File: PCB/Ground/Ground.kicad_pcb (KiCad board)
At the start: 2 copper layers, 100 x 86.6 mm, 39 parts, among them CN1 GROVE, CN2 GROVE, CN3 GROVE, CN4 GROVE, CN5 GROVE, CN6 TTL-232R-3V3, CN7 ST-LINK, CN8 Conn_01x05_Female, CN9 CardEdgeConnector5P, SW1 RESET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

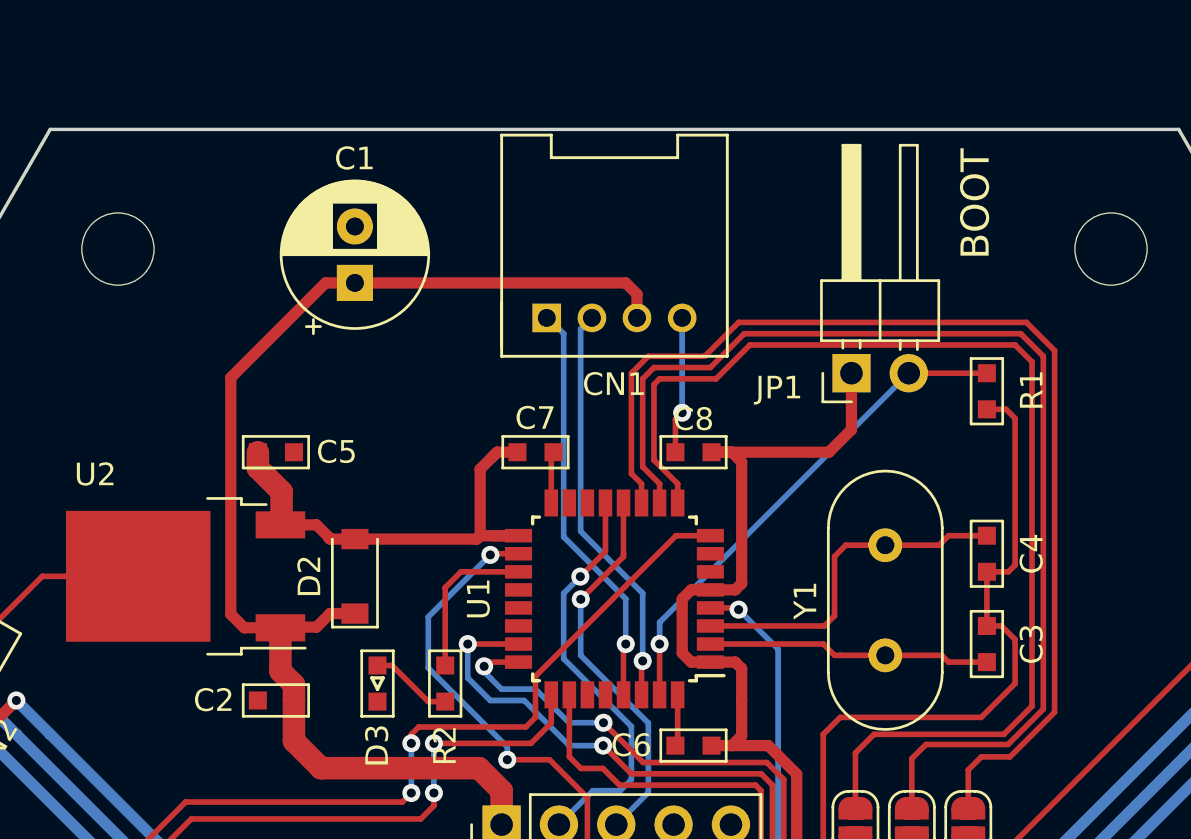
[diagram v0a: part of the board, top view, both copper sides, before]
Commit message: [update] Groundの配線改善(+5V配線, BOOT) #4
* C5(レギュレータ直近)を反転
* +5V配線幅を0.5mmから1.0mmに拡大
* JP1(BOOT)にOPEN/SHORTそれぞれの機能をシルクで記載
  (RUN/BOOT)
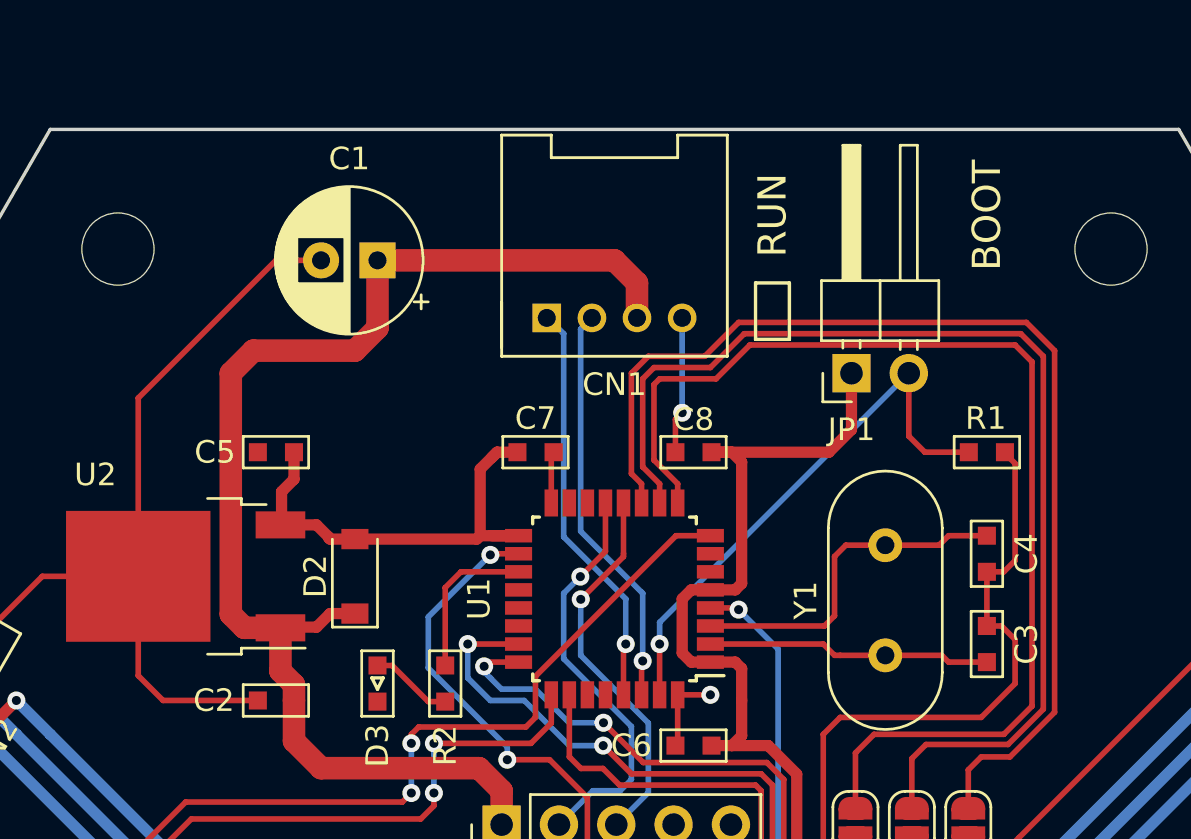
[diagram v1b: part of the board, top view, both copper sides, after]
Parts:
- moved R1 2.70 mm to (146.5, 76.0), turned to 0 degrees
- moved C1 1.41 mm to (119.5, 67.5), turned to 180 degrees
- turned C5 to 180 degrees
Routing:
- net GND: track 116.5 -> 143.8 mm, vias 1 -> 2
- net 5V: track 220.4 -> 223.4 mm
- net Net-(JP1-Pad2): track 22.3 -> 24.6 mm
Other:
- board text added: "RUN"

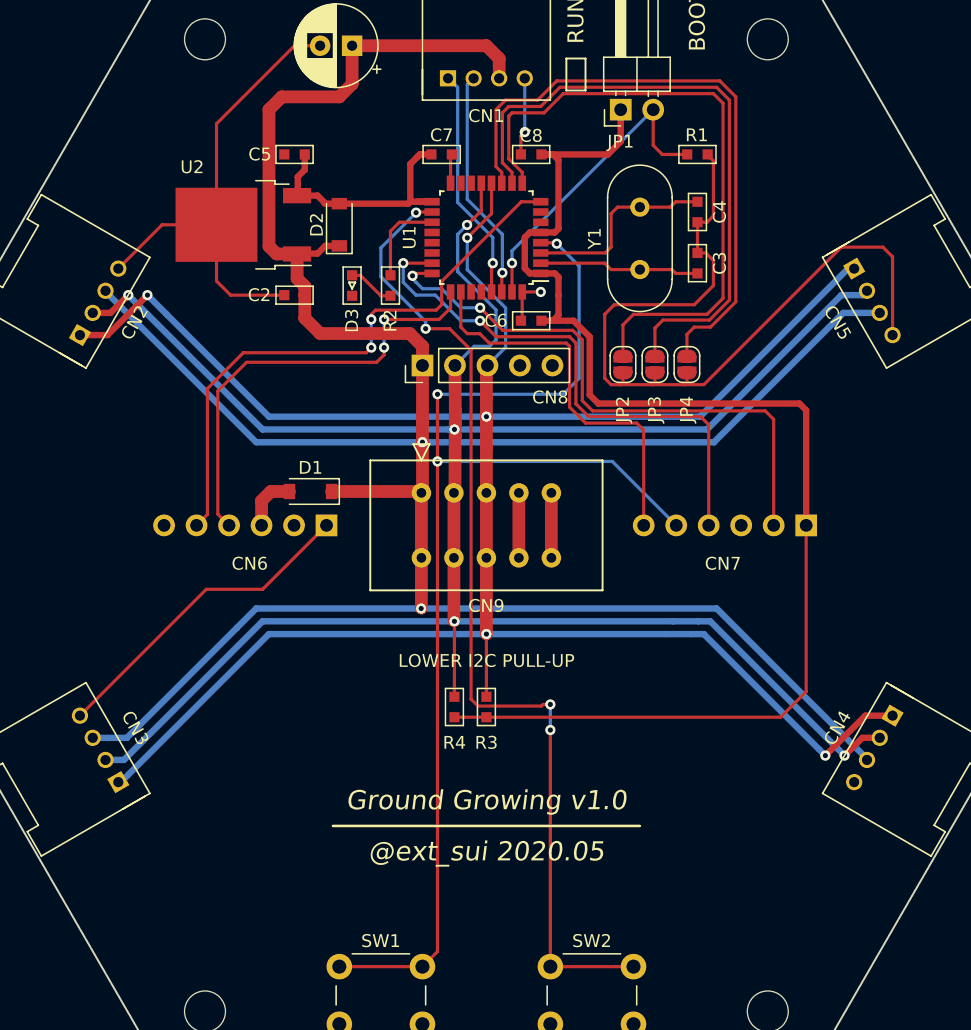
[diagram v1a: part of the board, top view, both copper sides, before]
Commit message: [update] Groundの配線改善(3V3配線, シルク) #4
* IC周辺の3V3配線を他の配線より優先するように修正
* I2C関連のコネクタ部の裏側にシルクを追加
* JP2-4の配線を表面から裏面に変更し配線長を短縮
* ST-LINK関連の配線を下に移動しGNDベタ用ビアを追加
* IC周辺のビア位置を整頓
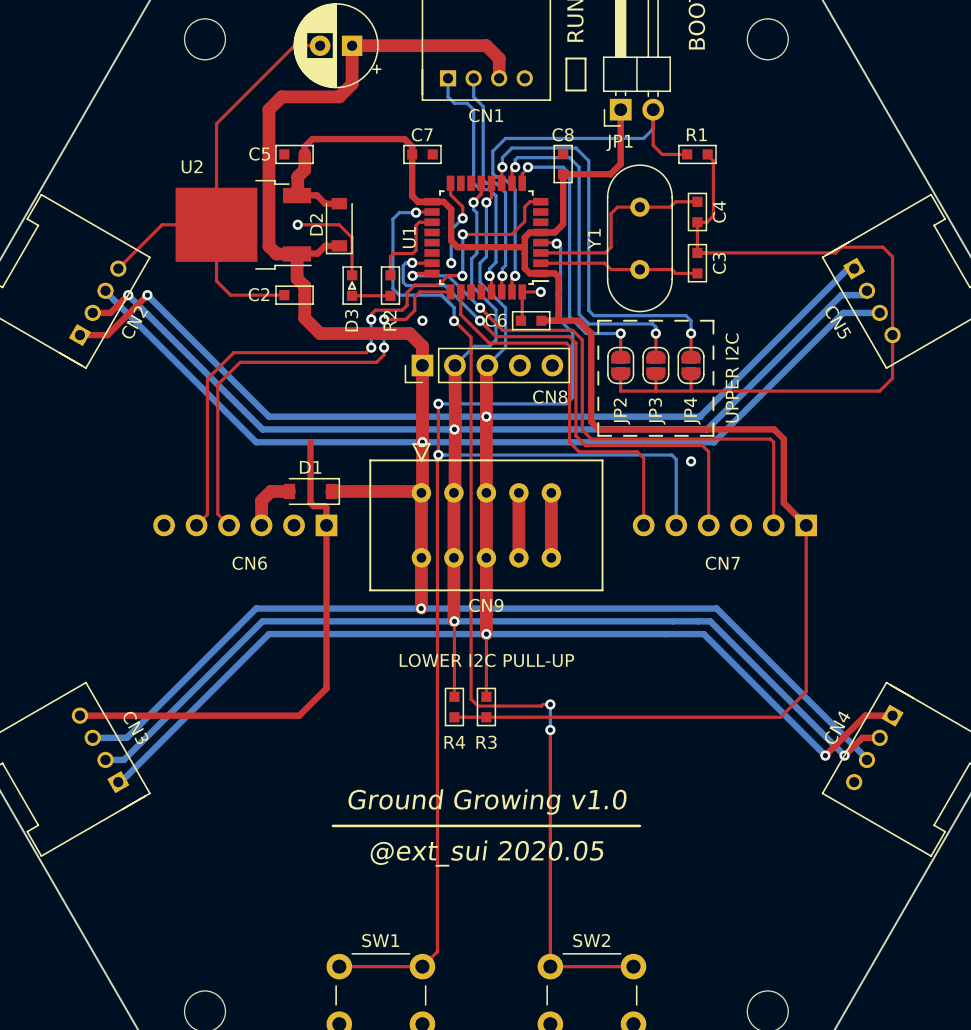
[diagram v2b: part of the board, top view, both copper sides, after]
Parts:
- moved C8 2.61 mm to (136.0, 76.8), turned to 270 degrees
- moved C7 1.50 mm to (125.0, 76.0)
- moved JP4 0.33 mm to (146.0, 92.5)
- moved JP2 0.19 mm to (140.5, 92.5)
- moved JP3 0.11 mm to (143.2, 92.5)
- turned D3 to 270 degrees
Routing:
- net Net-(JP2-Pad2): track 49.9 -> 22.4 mm, vias 0 -> 2
- net Net-(JP3-Pad2): track 49.4 -> 27.6 mm, vias 0 -> 2
- net GND: track 143.8 -> 162.9 mm, vias 2 -> 6
- net Net-(JP4-Pad2): track 48.7 -> 32.3 mm, vias 0 -> 2
- net 3V3: track 124.8 -> 133.2 mm
- net Net-(JP1-Pad2): track 24.6 -> 32.6 mm
- net NRST: track 96.6 -> 99.4 mm
- net RXD: track 45.7 -> 48.3 mm, vias 2 -> 4
- net Net-(SW2-Pad1): track 78.0 -> 80.1 mm
- net UPPER_SCL: track 18.2 -> 19.5 mm
- net Net-(D3-Pad2): track 3.66 -> 3.00 mm
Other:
- board text added: "5"
- board text added: "D"
- board text added: "G"
- board text added: "S"
- board text added: "UPPER I2C"
- board text added: "×"

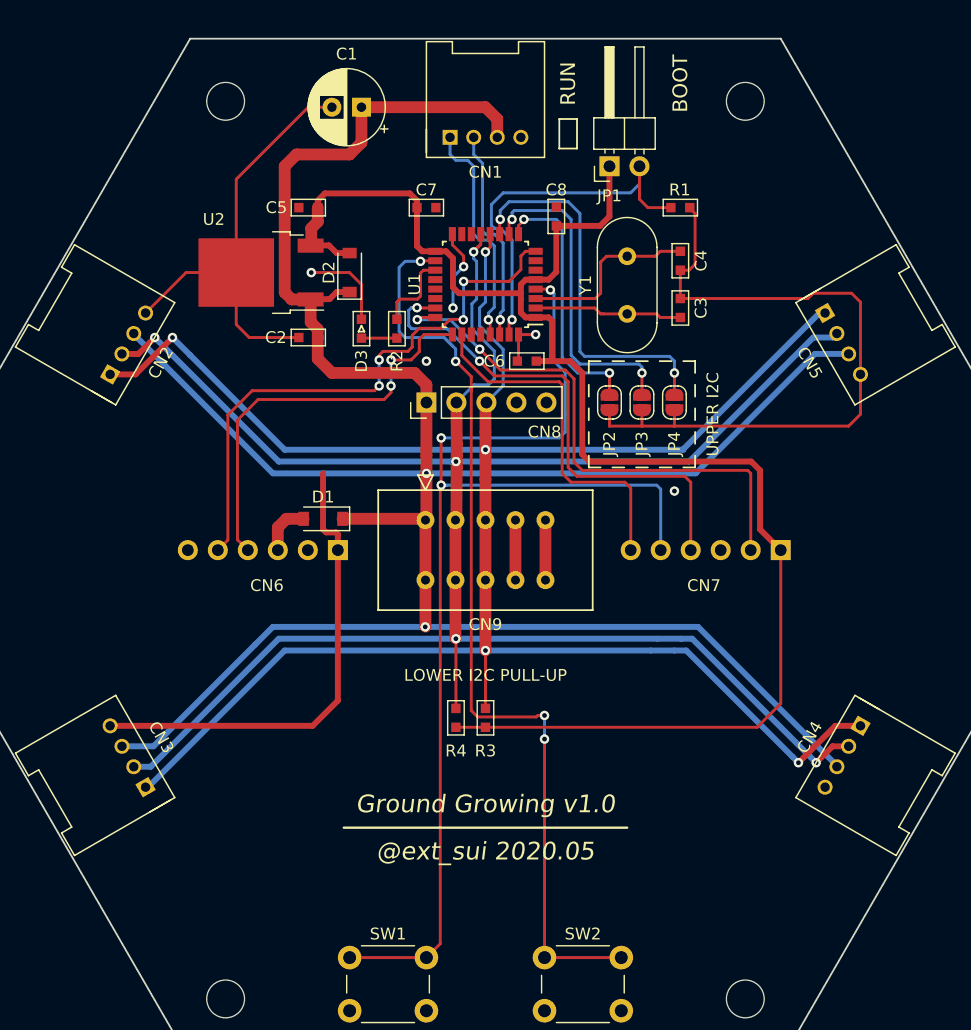
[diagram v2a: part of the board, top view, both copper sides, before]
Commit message: [update] Groundの配線改善(SW, PULL-UP) #4
* SW1,2の配線を表面から裏面に移動
* LOWER I2C PULL-UP を JP2-4 に合わせるために基板左上に移動
* カードエッジコネクタとの距離を離すためにD1の位置を移動
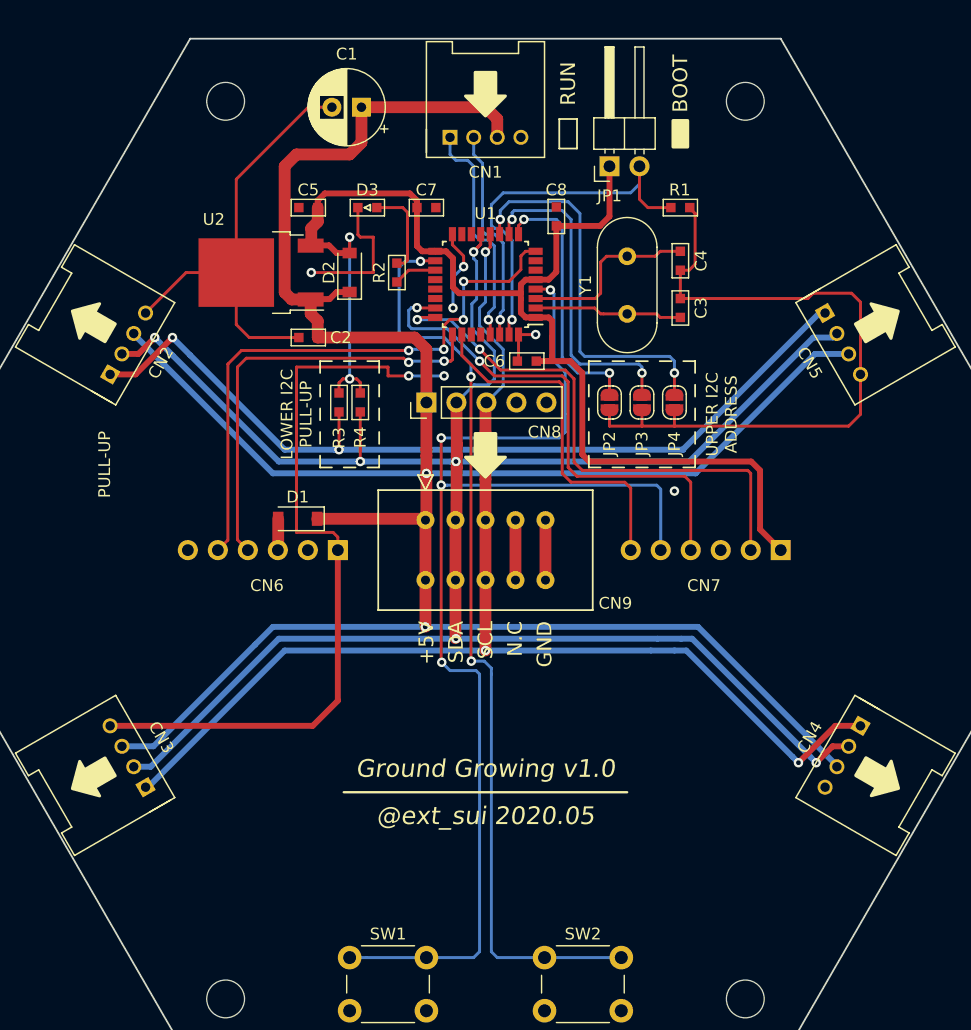
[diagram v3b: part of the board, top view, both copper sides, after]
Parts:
- moved R3 29.4 mm to (117.6, 92.5), turned to 270 degrees
- moved R4 27.9 mm to (119.4, 92.5), turned to 270 degrees
- moved D3 10.3 mm to (120.0, 76.0), turned to 0 degrees
- moved R2 4.75 mm to (122.5, 81.5), turned to 90 degrees
- moved D1 2.15 mm to (114.1, 102.3)
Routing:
- net GND: track 162.9 -> 191.7 mm, vias 6 -> 7
- net 3V3: track 133.2 -> 109.0 mm, vias 0 -> 2
- net NRST: track 99.4 -> 105.9 mm, vias 3 -> 4
- net Net-(D3-Pad2): track 3.00 -> 7.82 mm
- net Net-(R2-Pad1): track 6.96 -> 3.66 mm
- net 5V: track 223.4 -> 226.3 mm
- net TXD: track 34.8 -> 36.7 mm
- net Net-(CN6-Pad3): track 4.40 -> 2.66 mm
- net LOWER_SCL: track 184.5 -> 182.8 mm, vias 5 -> 6
- net LOWER_SDA: track 184.2 -> 182.5 mm, vias 5 -> 6
- net RXD: track 48.3 -> 49.9 mm
- net Net-(SW2-Pad1): track 80.1 -> 79.4 mm, vias 4 -> 3
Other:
- board text added: "N.C"
- board text added: "PULL-UP"
- board text added: "SCL"
- board text added: "SDA"
- board text added: "UPPER I2C ADDRESS"
- board text removed: "UPPER I2C"
